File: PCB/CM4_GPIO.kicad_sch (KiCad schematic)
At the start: 35 parts, among them CN1 DF40C-100DS-0.4V(51), J1 Micro_SD_Card_Det, J2 Conn_01x02_Pin, U2 74LVC1G07SE-7, U21 QG2439S, U4 RT9742GGJ5

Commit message: Added Primary and Secondary EEPROM
This will be used to store configuration separate from the OS.
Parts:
- added U6, U7: M24C64-WMN6TP, PARTS:SOIC-8_L5.0-W4.0-P1.27-LS6.0-BL, symbol PARTS:M24C64-WMN6TP
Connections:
- net +3.3v: now also U6.1 (E0), U6.2 (E1), U6.3 (E2), U6.8 (VCC), U7.1 (E0), U7.2 (E1), U7.3 (E2), U7.8 (VCC)
- net GND: now also U6.4 (VSS), U7.4 (VSS)
- net GPIO21: now also U7.7 (~{WC})
- net GPIO25: now also U6.7 (~{WC})
- net ID_SC: now also U7.6 (SCL)
- net ID_SD: now also U7.5 (SDA)
- net SCL0: now also U6.6 (SCL)
- net SDA0: now also U6.5 (SDA)
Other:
- note added: "64Kbit EEProm [Primary]"
- note added: "64Kbit EEProm [Secondary]"
- note added: "Ethernet Chassis -> GND"
- note added: "MII -> Ethernet Magnetics -> Ethernet Connector"
- note added: "POE_IN Diode Bridge"
- note removed: "A button between pins 13-14 can be used to wake up compute module from power down"
- note removed: "If compute modules is awake RUN_PG will be high so the button doesn't do anything If the compute module is asleep then RUN_PG will be at 0v and so pull global enable low"
- note removed: "POE_IN"
- moved on the sheet: C1, C2, C3, C4, C5, C77, D1, D11, D2, FB13, J1, J2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

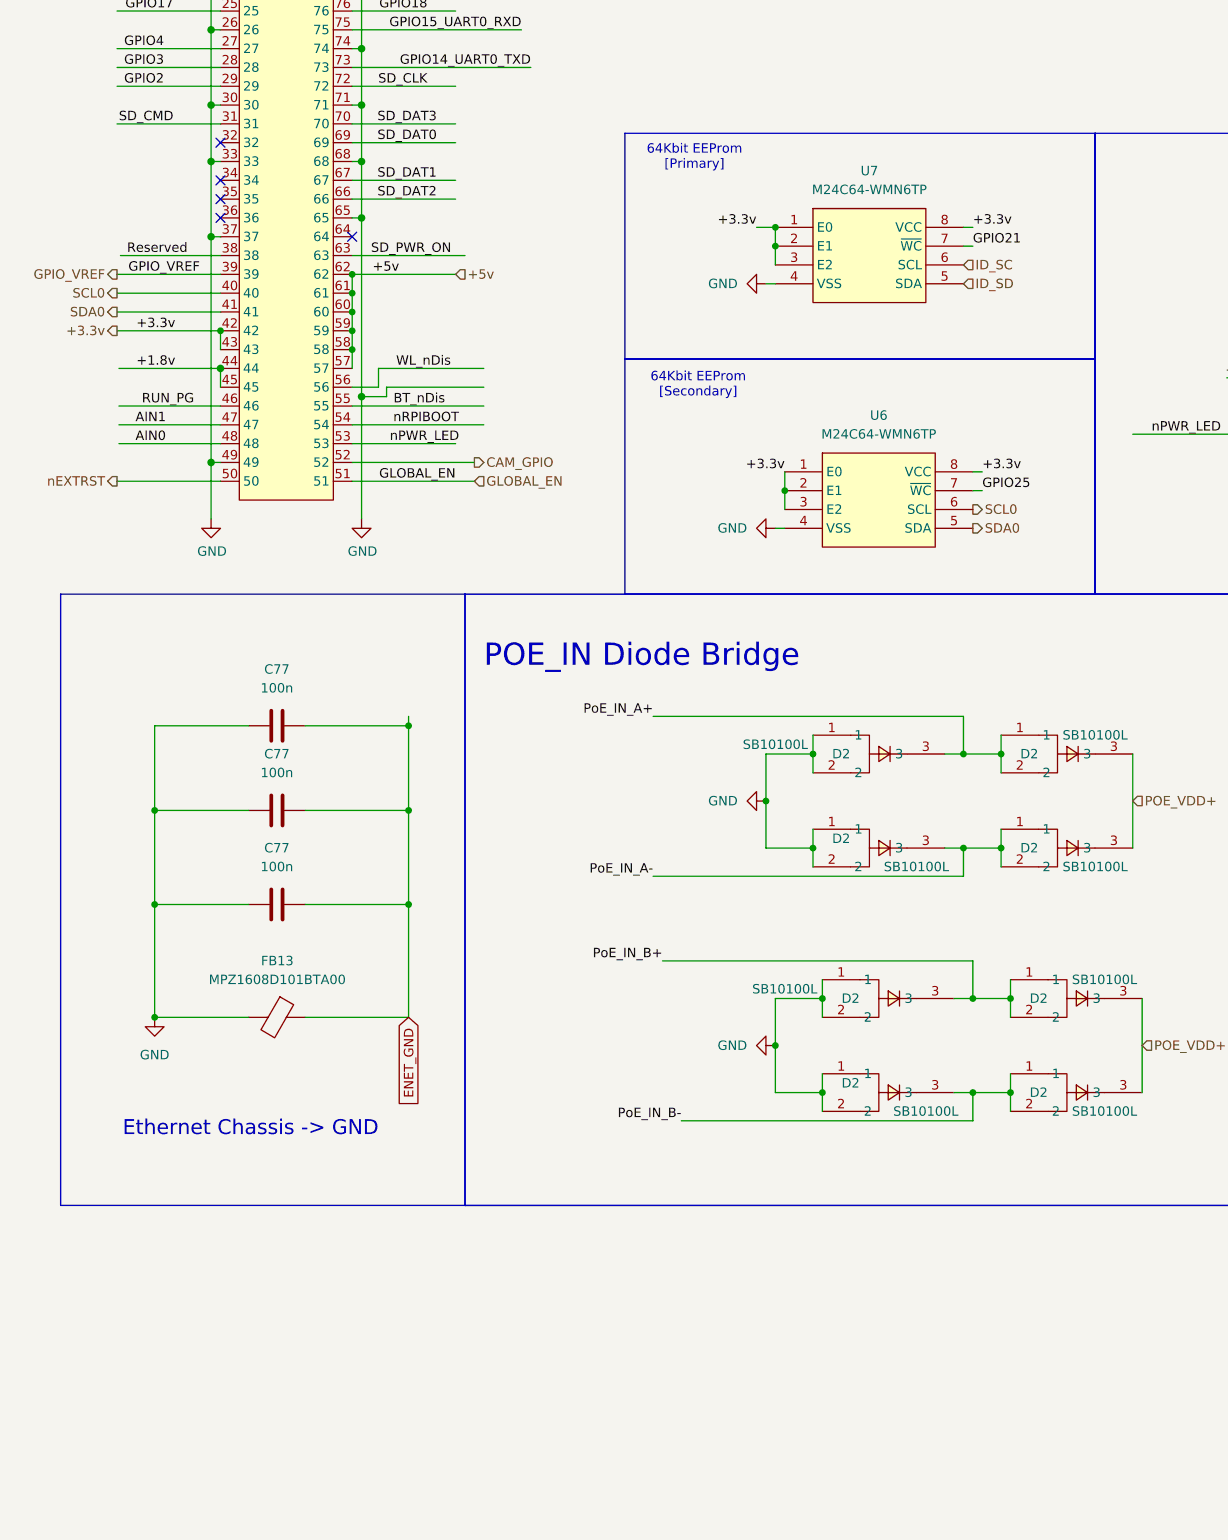
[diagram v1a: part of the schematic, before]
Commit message: Had to go with an inverting buffer, to correctly setup the EEPROM
The WC pin of the eeprom, disables writing when it is high. Default state has GPIO 25, and GPIO21 are pulled low.

I want the EEPROM to disable writing until I am ready to write to it.

During normal Pi Operation (GPIOlow) the eeprom is in the following state:

Input A(+3.3V) = HIGH
INPUT /G (GPIO) = LOW
Output Y = LOW

And when GPIO goes high, it is left floating, so writing can happen.

Input A(+3.3V) = HIGH
INPUT /G (GPIO) = HIGH
Output Y = FLOAT
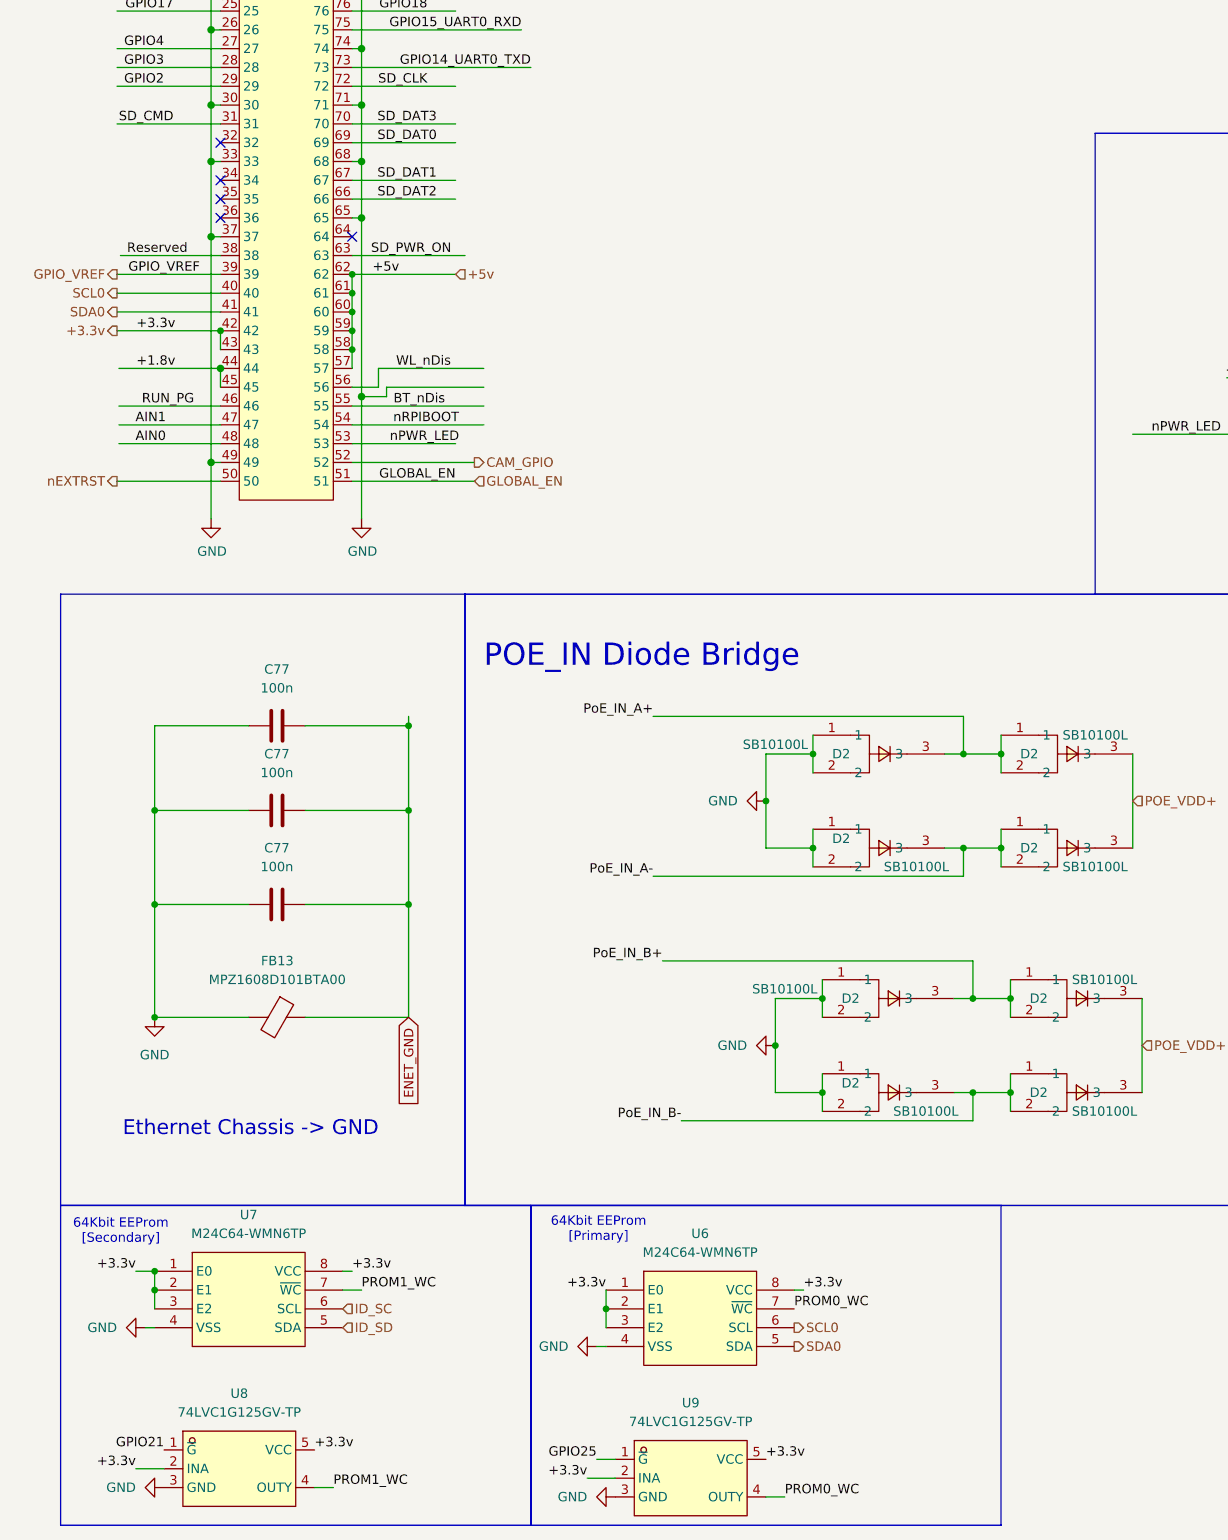
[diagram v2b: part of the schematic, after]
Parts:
- added U8, U9: 74LVC1G125GV-TP, PARTS:SOT-23-5_L2.9-W1.6-P0.95-LS2.8-BR, symbol PARTS:74LVC1G125GV-TP
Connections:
- net +3.3v: now also U8.2 (INA), U8.5 (VCC), U9.2 (INA), U9.5 (VCC)
- net GND: now also U8.3 (GND), U9.3 (GND)
- net GPIO21: now also U8.1 (~{G}); no longer U7.7 (~{WC})
- net GPIO25: now also U9.1 (~{G}); no longer U6.7 (~{WC})
- new net PROM0_WC: U6.7 (~{WC}), U9.4 (OUTY)
- new net PROM1_WC: U7.7 (~{WC}), U8.4 (OUTY)
